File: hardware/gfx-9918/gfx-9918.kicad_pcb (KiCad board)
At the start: 2 copper layers, 50 x 150 mm, 28 parts, among them J1 GFX_Connector_Input, J2 AV, J3 Sound L, J4 Sound R, U1 TMS9918, U2 74HCT04, U3 74HCT574, U4 74HCT574, U5 74HCT574, U6 HM62256ALP-10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

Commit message: [gfx9918] Fix capacitor values for clock circuit
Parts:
- C1, C2: value 27pF -> 56pF
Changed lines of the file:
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@@
       (effects (font (size 1 1) (thickness 0.15)))
     )
-    (fp_text value 27pF (at 1.23 2.54) (layer F.Fab)
+    (fp_text value 56pF (at 1.23 2.54) (layer F.Fab)
       (effects (font (size 1 1) (thickness 0.15)))
     )
@@
       (effects (font (size 1 1) (thickness 0.15)))
     )
-    (fp_text value 27pF (at 1.27 -2.54 180) (layer F.Fab)
+    (fp_text value 56pF (at 1.27 -2.54 180) (layer F.Fab)
       (effects (font (size 1 1) (thickness 0.15)))
     )

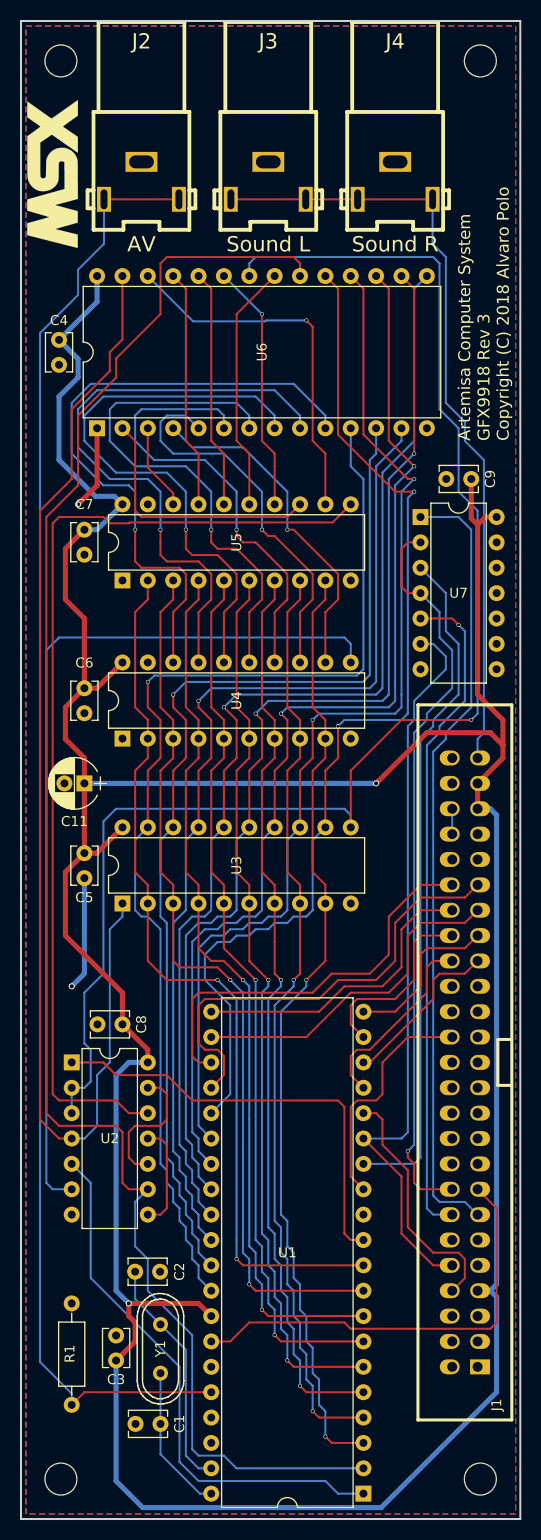
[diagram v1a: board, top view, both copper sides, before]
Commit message: [gfx9918] Set board settings to match JCLPCB design rules
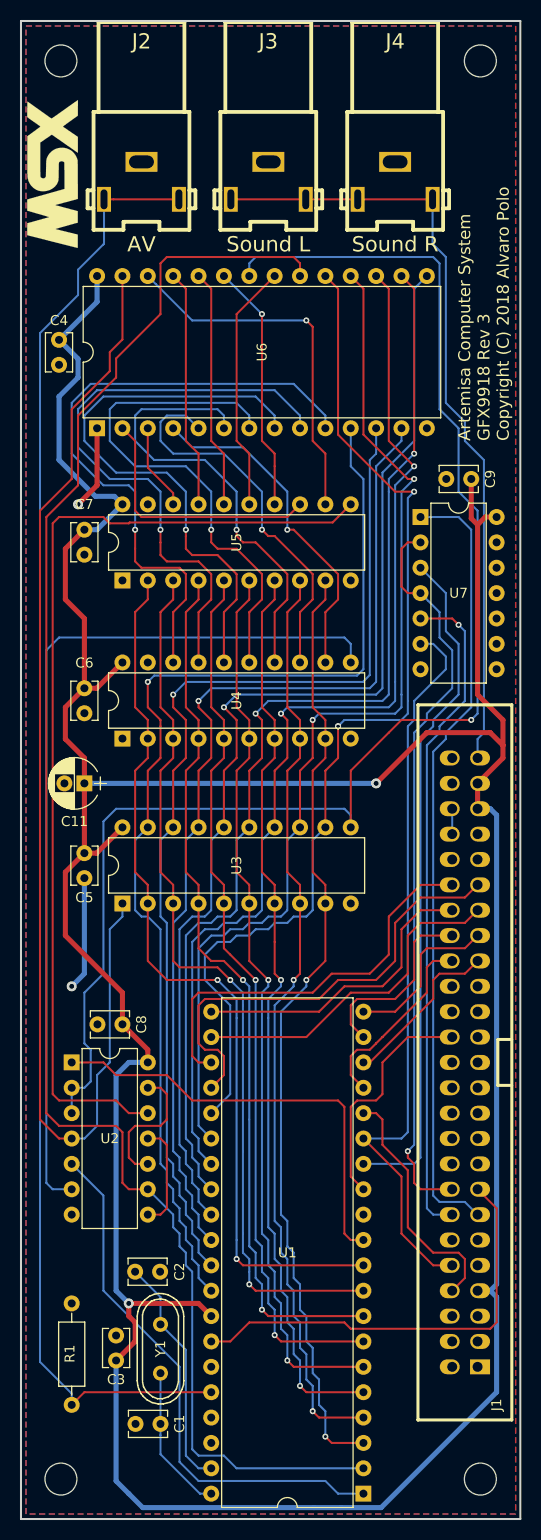
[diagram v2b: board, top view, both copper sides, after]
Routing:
- net /~CAS: track 168.7 -> 167.7 mm
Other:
- net class Default: via_dia 0.4064 -> 0.6; via_drill 0.3048 -> 0.3
- net class Power: via_dia 0.6096 -> 1; via_drill 0.4064 -> 0.5
- rule via_min_drill: 0.3048 -> 0.3
- rule via_min_size: 0.4064 -> 0.6

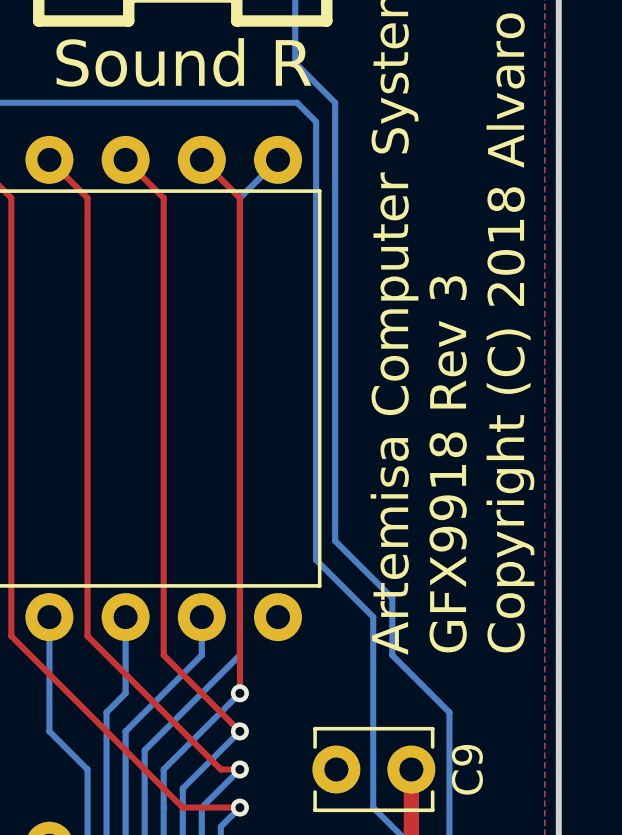
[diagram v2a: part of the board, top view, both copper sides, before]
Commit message: Update changelogs and revision numbers of all PCBs
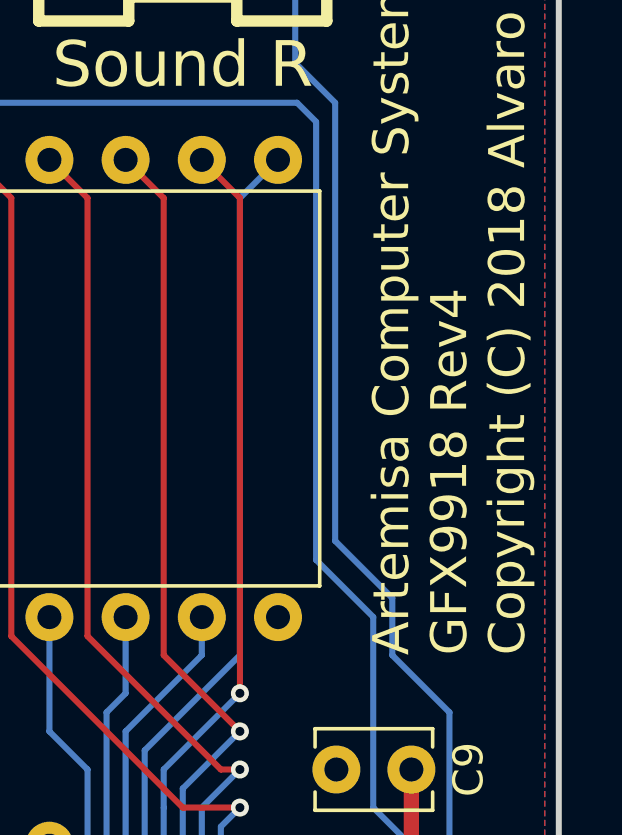
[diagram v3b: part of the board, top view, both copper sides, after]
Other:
- board text added: "Artemisa Computer System GFX9918 Rev4 Copyright (C) 2018 Alvaro Polo"
- board text removed: "Artemisa Computer System GFX9918 Rev 3 Copyright (C) 2018 Alvaro Polo"
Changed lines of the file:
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@@
       (xy -5.472572 -2.546406)) (layer F.SilkS) (width 0.01))
   )
-  (gr_text "Artemisa Computer System\nGFX9918 Rev 3\nCopyright (C) 2018 Alvaro Polo" (at 90.355 80.05 90) (layer F.SilkS)
+  (gr_text "Artemisa Computer System\nGFX9918 Rev4\nCopyright (C) 2018 Alvaro Polo" (at 90.355 80.05 90) (layer F.SilkS)
     (effects (font (size 1.2 1.2) (thickness 0.2)) (justify left))
   )

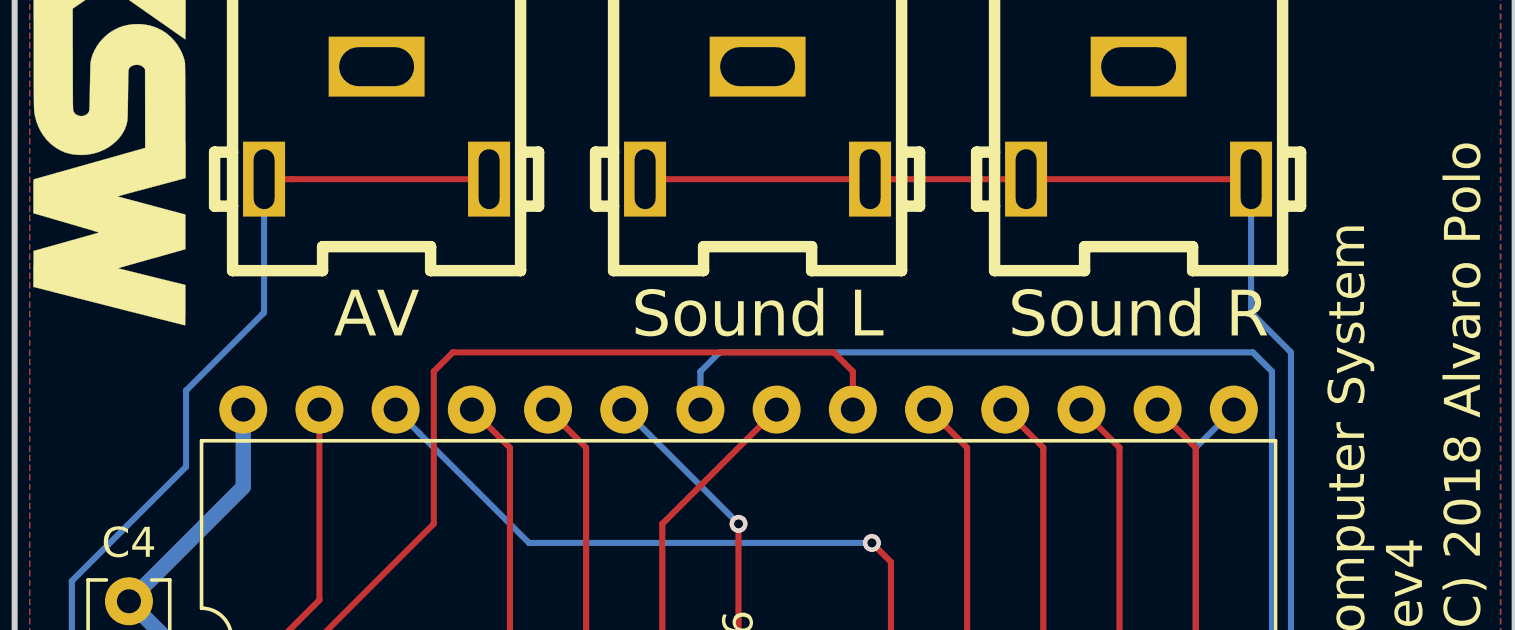
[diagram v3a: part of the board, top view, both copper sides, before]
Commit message: Fix background color issues by unconnecting EXTVDP pin
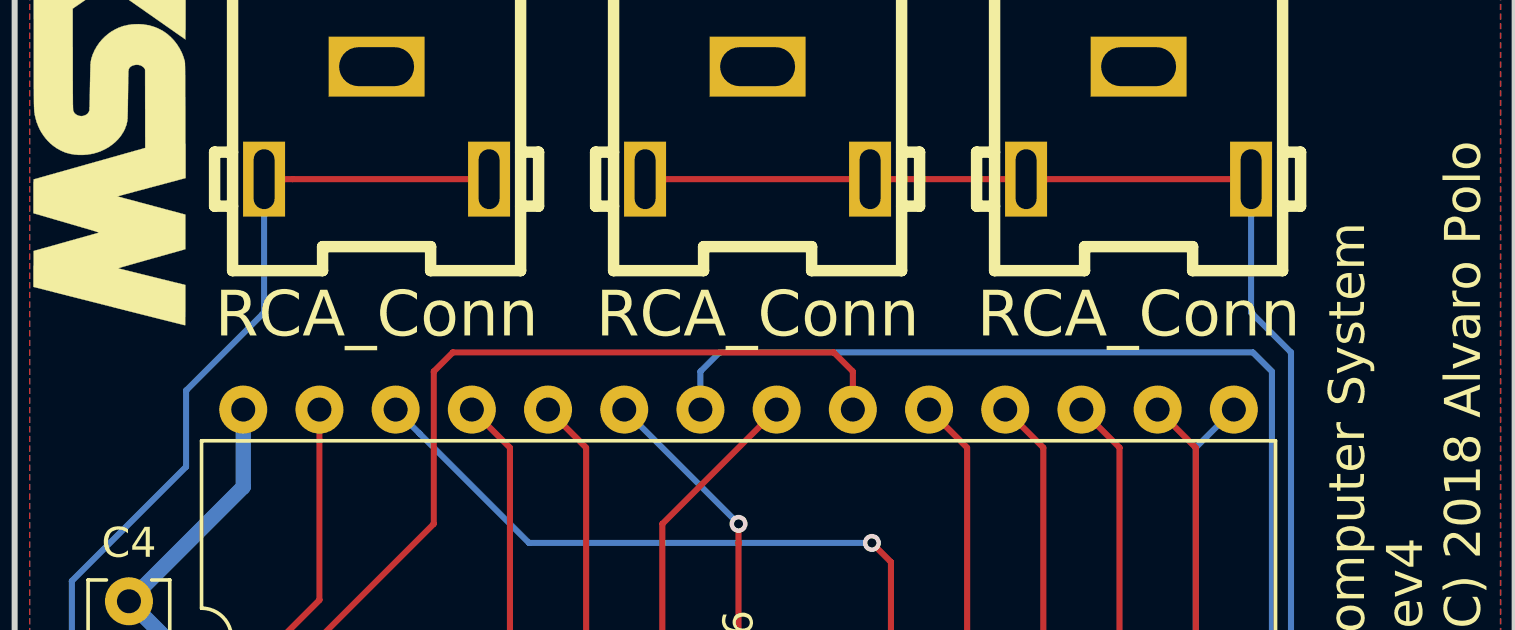
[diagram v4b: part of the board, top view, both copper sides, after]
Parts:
- J2: value AV -> RCA_Conn
- J3: value Sound L -> RCA_Conn
- J4: value Sound R -> RCA_Conn
- U6: value HM62256ALP-10 -> 62256
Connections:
- U1 pad 35: GND -> Net-(U1-Pad35)
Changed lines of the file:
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@@
     (zones 0)
     (modules 28)
-    (nets 96)
+    (nets 97)
   )
   (page A4)
@@
   (net 94 /SOUNDOUT)
   (net 95 ~)
+  (net 96 "Net-(U1-Pad35)")
   (net_class Default "Esta es la clase de red por defecto."
     (clearance 0.2032)
@@
     (add_net "Net-(U1-Pad11)")
     (add_net "Net-(U1-Pad14)")
+    (add_net "Net-(U1-Pad35)")
     (add_net "Net-(U1-Pad37)")
     (add_net "Net-(U1-Pad38)")
@@
       (effects (font (size 1 1) (thickness 0.15)))
     )
-    (fp_text value HM62256ALP-10 (at 7.62 35.41 90) (layer F.Fab)
+    (fp_text value 62256 (at 7.62 35.41 90) (layer F.Fab)
       (effects (font (size 1 1) (thickness 0.15)))
     )
@@
       (net 40 /~IRQ))
     (pad 35 thru_hole oval (at 15.24 12.7 180) (size 1.6 1.6) (drill 0.8) (layers *.Cu *.Mask)
-      (net 2 GND))
+      (net 96 "Net-(U1-Pad35)"))
     (pad 15 thru_hole oval (at 0 35.56 180) (size 1.6 1.6) (drill 0.8) (layers *.Cu *.Mask)
       (net 39 /~CSR))
@@
       (effects (font (size 1.524 1.524) (thickness 0.3048)))
     )
-    (fp_text value "Sound R" (at 0 -8.255 180) (layer F.SilkS)
+    (fp_text value RCA_Conn (at 0 -8.255 180) (layer F.SilkS)
       (effects (font (size 1.524 1.524) (thickness 0.3048)))
     )
@@
       (effects (font (size 1.524 1.524) (thickness 0.3048)))
     )
-    (fp_text value "Sound L" (at 0 -8.255 180) (layer F.SilkS)
+    (fp_text value RCA_Conn (at 0 -8.255 180) (layer F.SilkS)
       (effects (font (size 1.524 1.524) (thickness 0.3048)))
     )
@@
       (effects (font (size 1.524 1.524) (thickness 0.3048)))
     )
-    (fp_text value AV (at 0 -8.255 180) (layer F.SilkS)
+    (fp_text value RCA_Conn (at 0 -8.255 180) (layer F.SilkS)
       (effects (font (size 1.524 1.524) (thickness 0.3048)))
     )
